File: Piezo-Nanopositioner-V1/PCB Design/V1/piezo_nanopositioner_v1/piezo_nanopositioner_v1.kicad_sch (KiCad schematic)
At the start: 11 parts, among them J101 Conn_01x03_Pin

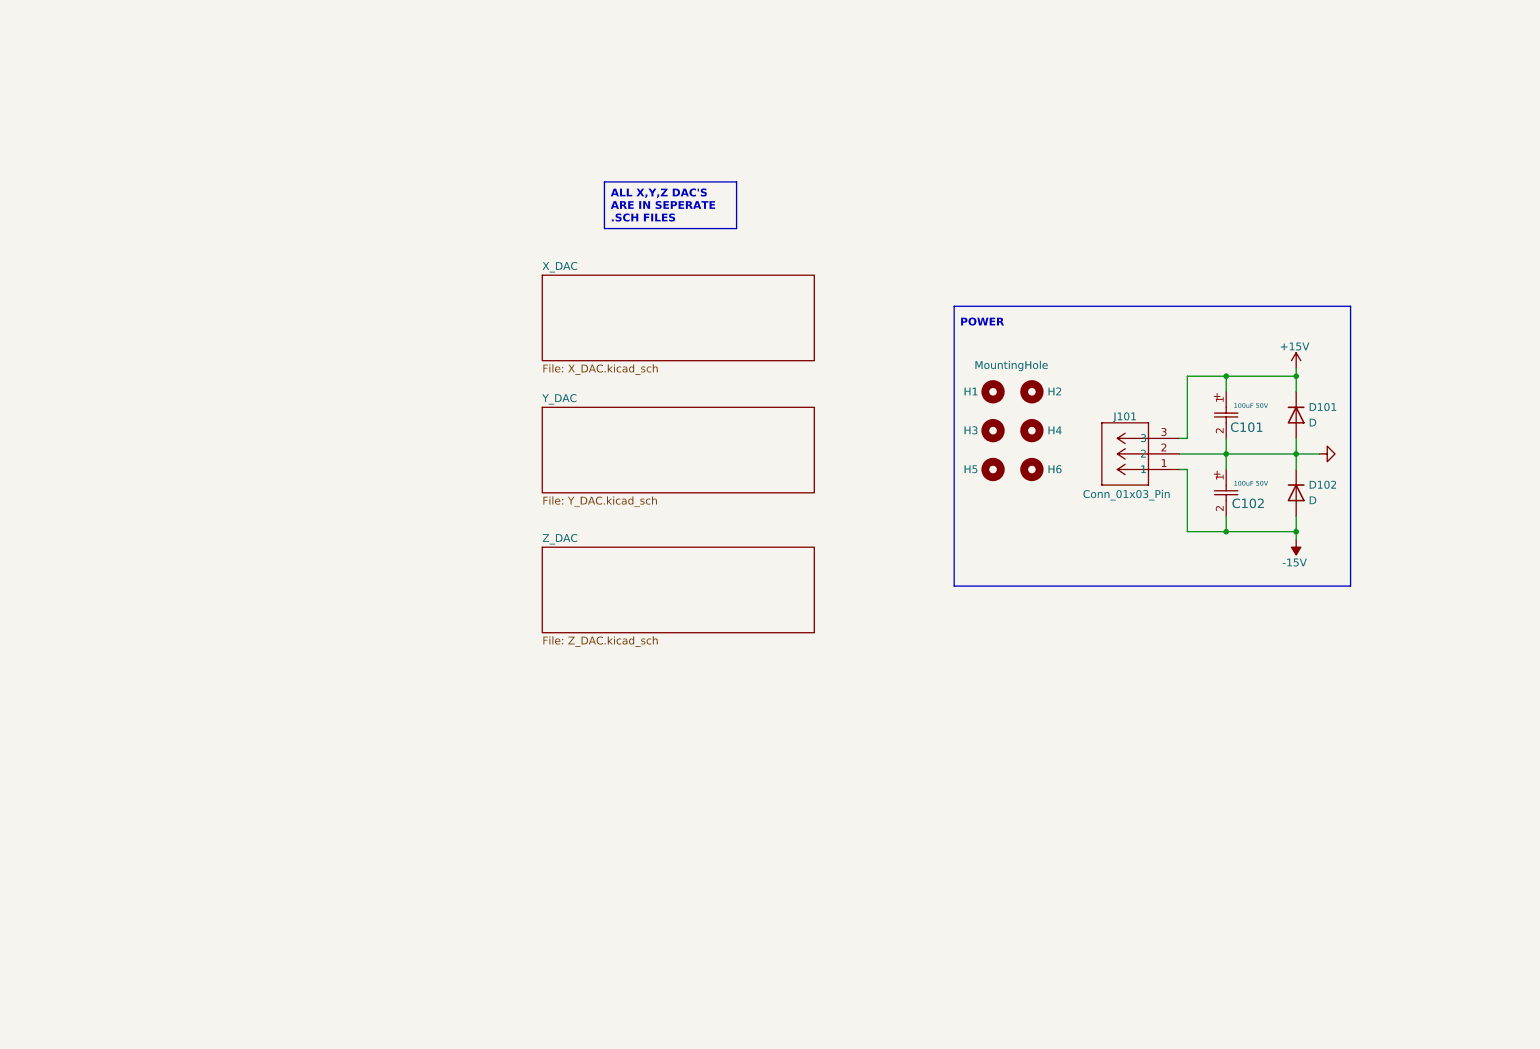
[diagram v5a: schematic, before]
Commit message: deleted unused files
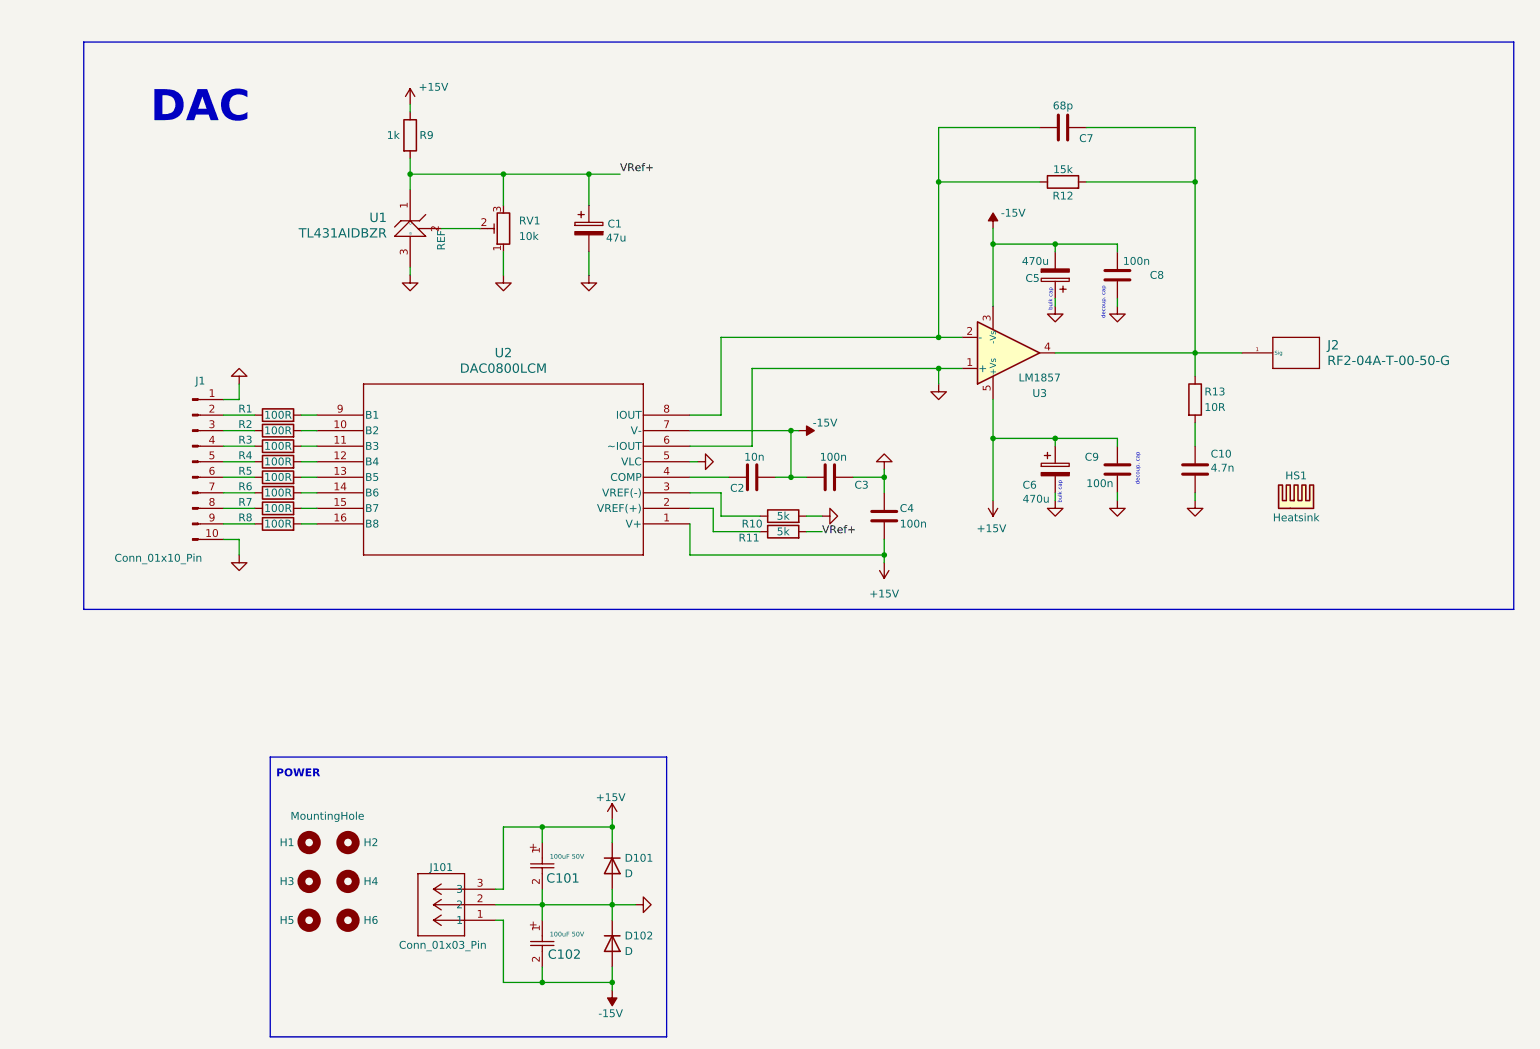
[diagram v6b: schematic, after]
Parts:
- added C1: 47u, Capacitor_SMD:CAP_EEFC_E_PAN, symbol Device:C_Polarized
- added C10: 4.7n, Capacitor_SMD:C_0805_2012Metric, symbol Device:C
- added C2: 10n, Capacitor_SMD:C_0805_2012Metric, symbol Device:C
- added C3, C4, C8, C9: 100n, Capacitor_SMD:C_0805_2012Metric, symbol Device:C
- added C5, C6: 470u, Capacitor_THT:CAP_ZSU_G12_PAN, symbol Device:C_Polarized
- added C7: 68p, Capacitor_SMD:C_0805_2012Metric, symbol Device:C
- added HS1: Heatsink, V6560Y:V6560Y, symbol Mechanical:Heatsink
- added J1: Conn_01x10_Pin, Connector_PinHeader_2.54mm:PinHeader_1x10_P2.54mm_Vertical, symbol Connector:Conn_01x10_Pin
- added J2: RF2-04A-T-00-50-G, CONN_RF2-04A-T-00-50-G_ADM, symbol SMA_Connector:RF2-04A-T-00-50-G
- added R1, R2, R3, R4, R5, R6, R7, R8: 100R, Resistor_SMD:R_0805_2012Metric, symbol Device:R
- added R10, R11: 5k, Resistor_SMD:R_0805_2012Metric, symbol Device:R
- added R12: 15k, Resistor_SMD:R_0805_2012Metric, symbol Device:R
- added R13: 10R, Resistor_SMD:R_0805_2012Metric, symbol Device:R
- added R9: 1k, Resistor_SMD:R_0805_2012Metric, symbol Device:R
- added RV1: 10k, Potentiometer_THT:TRIM_COM-09806, symbol Device:R_Potentiometer_Trim
- added U1: TL431AIDBZR, DBZ0003A_N, symbol TL431AIDBZR:TL431AIDBZR
- added U2: DAC0800LCM, M16A_TEX, symbol DAC0800LCM_SMT:DAC0800LCM
- added U3: LM1857, Package_TO_SOT_THT:TO-220-5_P3.4x3.7mm_StaggerOdd_Lead3.8mm_Vertical, symbol Amplifier_Audio:TDA2050
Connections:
- net +15V: now also C4.2, C6.1, C9.1, R9.1, U2.1 (V+), U3.5 (+Vs)
- net -15V: now also C2.2, C3.1, C5.2, C8.2, U2.7 (V-), U3.3 (-Vs)
- net GND: now also C1.2, C10.2, C3.2, C4.1, C5.1, C6.2, C8.1, C9.2, J1.1 (Pin_1), J1.10 (Pin_10), R10.2, RV1.1, U1.3 (a), U2.5 (VLC), U2.6 (~IOUT), U3.1 (+)
- new net: C7.2, J2.1 (Sig), R12.2, R13.1, U3.4
- new net: C10.1, R13.2
- new net: J1.8 (Pin_8), R7.1
- new net: R7.2, U2.15 (B7)
- new net: R2.2, U2.10 (B2)
- new net: R3.2, U2.11 (B3)
- new net: R4.2, U2.12 (B4)
- new net: R5.2, U2.13 (B5)
- new net: R6.2, U2.14 (B6)
- new net: R8.2, U2.16 (B8)
- new net: R11.1, U2.2 (VREF(+))
- new net: R10.1, U2.3 (VREF(-))
- new net: C2.1, U2.4 (COMP)
- new net: C7.1, R12.1, U2.8 (IOUT), U3.2 (-)
- new net: R1.2, U2.9 (B1)
- new net: RV1.2, U1.2 (REF)
- new net: J1.2 (Pin_2), R1.1
- new net: J1.3 (Pin_3), R2.1
- new net: J1.4 (Pin_4), R3.1
- new net: J1.5 (Pin_5), R4.1
- new net: J1.6 (Pin_6), R5.1
- new net: J1.7 (Pin_7), R6.1
- new net: J1.9 (Pin_9), R8.1
- new net VRef+: C1.1, R11.2, R9.2, RV1.3, U1.1 (c)
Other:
- removed sheet X_DAC
- removed sheet Y_DAC
- removed sheet Z_DAC
- note added: "DAC"
- note added: "bulk cap"
- note added: "decoup. cap"
- moved on the sheet: C101, C102, D101, D102, H1, H2, H3, H4, H5, H6, J101
